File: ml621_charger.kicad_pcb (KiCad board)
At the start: 2 copper layers, 12.2 x 14.5 mm, 9 parts, among them J1 Conn_01x05

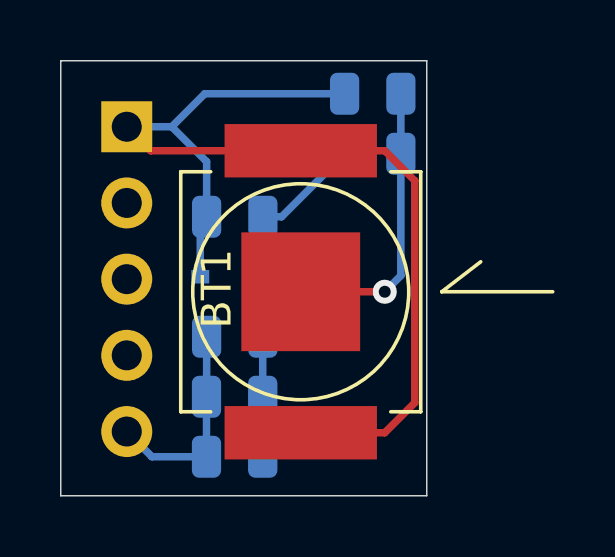
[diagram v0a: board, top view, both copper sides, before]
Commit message: Add schottkey diode to ensure reverse protection
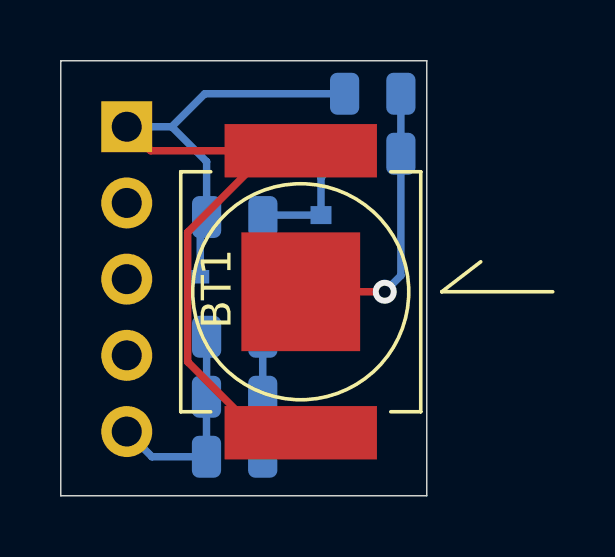
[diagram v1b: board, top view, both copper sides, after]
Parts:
- added D2: 500mV, Diode_SMD:D_SOD-523, B.Cu at (130.2, 93.3)
- R4: value 200R -> 100R
- R5: value 470R -> 330R
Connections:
- D1 pad 1: Net-(C1-Pad1) -> Net-(D1-Pad1)
- R1 pad 1: Net-(C1-Pad1) -> Net-(D1-Pad1)
- R2 pad 1: Net-(C1-Pad1) -> Net-(D1-Pad1)
- R3 pad 1: Net-(C1-Pad1) -> Net-(D1-Pad1)
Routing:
- net Net-(D1-Pad1): track 0.00 -> 8.20 mm
- net Net-(C1-Pad1): track 11.6 -> 4.35 mm
- net /GND: track 35.2 -> 33.4 mm

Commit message: Fix battery holder polarity
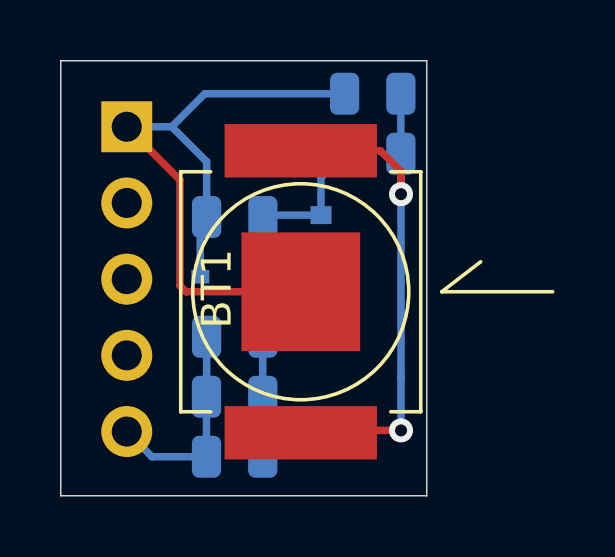
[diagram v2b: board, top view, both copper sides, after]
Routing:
- net Net-(BT1-Pad1): track 9.62 -> 21.4 mm, vias 1 -> 2
- net /GND: track 33.4 -> 23.4 mm
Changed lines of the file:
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@@
     (thickness 1.6)
     (drawings 4)
-    (tracks 36)
+    (tracks 42)
     (zones 0)
     (modules 10)
@@
     (add_net "Net-(J1-Pad4)")
   )
+  (module Battery:BatteryHolder_Keystone_2998_621_6.8x2.2mm (layer F.Cu)
+    (at 129.5 95.2 270)
+    (fp_text reference BT1 (at -0.1 2.8 90) (layer F.SilkS)
+      (effects (font (size 1 1) (thickness 0.15)))
+    )
+    (fp_text value ML621 (at 0.1 6.4 90) (layer F.Fab)
+      (effects (font (size 1 1) (thickness 0.15)))
+    )
+    (fp_line (start 4 4) (end 4 3) (layer F.SilkS) (width 0.12))
+    (fp_line (start -4 4) (end -4 3) (layer F.SilkS) (width 0.12))
+    (fp_line (start 4 -4) (end 4 -3) (layer F.SilkS) (width 0.12))
+    (fp_line (start -4 -4) (end -4 -3) (layer F.SilkS) (width 0.12))
+    (fp_line (start 0 -4.7) (end -1 -6) (layer F.SilkS) (width 0.12))
+    (fp_line (start 0 -8.4) (end 0 -4.7) (layer F.SilkS) (width 0.12))
+    (fp_line (start 4 4) (end -4 4) (layer F.SilkS) (width 0.12))
+    (fp_line (start -4 -4) (end 4 -4) (layer F.SilkS) (width 0.12))
+    (fp_circle (center 0 0) (end 3.6 0) (layer F.SilkS) (width 0.12))
+    (pad 1 smd rect (at 4.7 0 270) (size 1.78 5.08) (layers F.Cu F.Paste F.Mask)
+      (net 2 "Net-(BT1-Pad1)"))
+    (pad 1 smd rect (at -4.7 0 270) (size 1.78 5.08) (layers F.Cu F.Paste F.Mask)
+      (net 2 "Net-(BT1-Pad1)"))
+    (pad 2 smd rect (at 0 0 270) (size 3.96 3.96) (layers F.Cu F.Paste F.Mask)
+      (net 1 /GND))
+  )
   (module Diode_SMD:D_SOD-523 (layer B.Cu)
     (at 130.175 93.345 270)
@@
     )
   )
-  (module Battery:BatteryHolder_Keystone_2998_621_6.8x2.2mm (layer F.Cu)
-    (at 129.5 95.2 270)
-    (fp_text reference BT1 (at -0.1 2.8 90) (layer F.SilkS)
-      (effects (font (size 1 1) (thickness 0.15)))
-    )
-    (fp_text value ML621 (at 0.1 6.4 90) (layer F.Fab)
-      (effects (font (size 1 1) (thickness 0.15)))
-    )
-    (fp_line (start 4 4) (end 4 3) (layer F.SilkS) (width 0.12))
-    (fp_line (start -4 4) (end -4 3) (layer F.SilkS) (width 0.12))
-    (fp_line (start 4 -4) (end 4 -3) (layer F.SilkS) (width 0.12))
-    (fp_line (start -4 -4) (end -4 -3) (layer F.SilkS) (width 0.12))
-    (fp_line (start 0 -4.7) (end -1 -6) (layer F.SilkS) (width 0.12))
-    (fp_line (start 0 -8.4) (end 0 -4.7) (layer F.SilkS) (width 0.12))
-    (fp_line (start 4 4) (end -4 4) (layer F.SilkS) (width 0.12))
-    (fp_line (start -4 -4) (end 4 -4) (layer F.SilkS) (width 0.12))
-    (fp_circle (center 0 0) (end 3.6 0) (layer F.SilkS) (width 0.12))
-    (pad 2 smd rect (at 4.7 0 270) (size 1.78 5.08) (layers F.Cu F.Paste F.Mask)
-      (net 1 /GND))
-    (pad 2 smd rect (at -4.7 0 270) (size 1.78 5.08) (layers F.Cu F.Paste F.Mask)
-      (net 1 /GND))
-    (pad 1 smd rect (at 0 0 270) (size 3.96 3.96) (layers F.Cu F.Paste F.Mask)
-      (net 2 "Net-(BT1-Pad1)"))
-  )
   (module Resistor_SMD:R_0805_2012Metric (layer B.Cu)
     (at 131.9 88.6 180)
@@
   (gr_line (start 121.5 102) (end 133.7 102) (layer Edge.Cuts) (width 0.05))
   (gr_line (start 121.5 87.5) (end 121.5 102) (layer Edge.Cuts) (width 0.05))
-  (segment (start 124.5 90.5) (end 123.7 89.7) (width 0.25) (layer F.Cu) (net 1))
-  (segment (start 129.5 90.5) (end 124.5 90.5) (width 0.25) (layer F.Cu) (net 1))
   (segment (start 125.2 89.7) (end 123.7 89.7) (width 0.25) (layer B.Cu) (net 1))
   (segment (start 126.3 88.6) (end 125.2 89.7) (width 0.25) (layer B.Cu) (net 1))
@@
   (segment (start 126.3625 90.8625) (end 125.2 89.7) (width 0.25) (layer B.Cu) (net 1))
   (segment (start 126.3625 92.71) (end 126.3625 90.8625) (width 0.25) (layer B.Cu) (net 1))
-  (segment (start 129.5 99.9) (end 128.094 99.9) (width 0.25) (layer F.Cu) (net 1))
-  (segment (start 128.094 99.9) (end 125.73 97.536) (width 0.25) (layer F.Cu) (net 1))
-  (segment (start 129.5 90.5) (end 128.448 90.5) (width 0.25) (layer F.Cu) (net 1))
-  (segment (start 125.73 93.218) (end 125.73 97.536) (width 0.25) (layer F.Cu) (net 1))
-  (segment (start 128.448 90.5) (end 125.73 93.218) (width 0.25) (layer F.Cu) (net 1))
-  (via (at 132.3 95.2) (size 0.8) (drill 0.4) (layers F.Cu B.Cu) (net 2))
-  (segment (start 129.5 95.2) (end 132.3 95.2) (width 0.25) (layer F.Cu) (net 2))
-  (segment (start 132.8375 94.6625) (end 132.3 95.2) (width 0.25) (layer B.Cu) (net 2))
-  (segment (start 132.8375 90.6) (end 132.8375 94.6625) (width 0.25) (layer B.Cu) (net 2))
+  (segment (start 129.5 95.2) (end 125.68 95.2) (width 0.25) (layer F.Cu) (net 1))
+  (segment (start 125.68 95.2) (end 125.476 94.996) (width 0.25) (layer F.Cu) (net 1))
+  (segment (start 125.476 91.476) (end 123.7 89.7) (width 0.25) (layer F.Cu) (net 1))
+  (segment (start 125.476 94.996) (end 125.476 91.476) (width 0.25) (layer F.Cu) (net 1))
+  (segment (start 129.5 99.9) (end 128.094 99.9) (width 0.25) (layer F.Cu) (net 2))
+  (segment (start 129.5 90.5) (end 128.448 90.5) (width 0.25) (layer F.Cu) (net 2))
   (segment (start 132.8375 90.6) (end 132.8375 88.6) (width 0.25) (layer B.Cu) (net 2))
+  (segment (start 129.5 90.5) (end 132.156 90.5) (width 0.25) (layer F.Cu) (net 2))
+  (via (at 132.842 91.948) (size 0.8) (drill 0.4) (layers F.Cu B.Cu) (net 2))
+  (segment (start 132.156 90.5) (end 132.842 91.186) (width 0.25) (layer F.Cu) (net 2))
+  (segment (start 132.842 91.186) (end 132.842 91.948) (width 0.25) (layer F.Cu) (net 2))
+  (segment (start 132.842 90.6045) (end 132.8375 90.6) (width 0.25) (layer B.Cu) (net 2))
+  (segment (start 132.842 91.948) (end 132.842 90.6045) (width 0.25) (layer B.Cu) (net 2))
+  (segment (start 132.842 91.948) (end 132.842 98.044) (width 0.25) (layer B.Cu) (net 2))
+  (via (at 132.842 99.822) (size 0.8) (drill 0.4) (layers F.Cu B.Cu) (net 2))
+  (segment (start 132.842 98.044) (end 132.842 99.822) (width 0.25) (layer B.Cu) (net 2))
+  (segment (start 129.578 99.822) (end 129.5 99.9) (width 0.25) (layer F.Cu) (net 2))
+  (segment (start 132.842 99.822) (end 129.578 99.822) (width 0.25) (layer F.Cu) (net 2))
   (segment (start 128.25 92.7125) (end 128.2375 92.7) (width 0.25) (layer B.Cu) (net 3))
   (segment (start 128.3025 92.645) (end 128.2375 92.71) (width 0.25) (layer B.Cu) (net 3))
@@
   (segment (start 130.175 91.3875) (end 130.9625 90.6) (width 0.25) (layer B.Cu) (net 3))
   (segment (start 130.175 92.645) (end 130.175 91.3875) (width 0.25) (layer B.Cu) (net 3))
+  (segment (start 124.54 100.7) (end 123.7 99.86) (width 0.25) (layer B.Cu) (net 4))
+  (segment (start 126.357499 100.7) (end 124.54 100.7) (width 0.25) (layer B.Cu) (net 4))
+  (segment (start 126.357499 98.7) (end 126.357499 100.7) (width 0.25) (layer B.Cu) (net 4))
+  (segment (start 126.3625 98.694999) (end 126.357499 98.7) (width 0.25) (layer B.Cu) (net 4))
+  (segment (start 126.3625 96.7) (end 126.3625 98.694999) (width 0.25) (layer B.Cu) (net 4))
   (segment (start 128.2375 94.7125) (end 128.25 94.7) (width 0.25) (layer B.Cu) (net 8))
   (segment (start 128.2375 96.7) (end 128.2375 94.7125) (width 0.25) (layer B.Cu) (net 8))
@@
   (segment (start 128.232499 96.705001) (end 128.2375 96.7) (width 0.25) (layer B.Cu) (net 8))
   (segment (start 128.232499 98.7) (end 128.232499 96.705001) (width 0.25) (layer B.Cu) (net 8))
-  (segment (start 124.54 100.7) (end 123.7 99.86) (width 0.25) (layer B.Cu) (net 4))
-  (segment (start 126.357499 100.7) (end 124.54 100.7) (width 0.25) (layer B.Cu) (net 4))
-  (segment (start 126.357499 98.7) (end 126.357499 100.7) (width 0.25) (layer B.Cu) (net 4))
-  (segment (start 126.3625 98.694999) (end 126.357499 98.7) (width 0.25) (layer B.Cu) (net 4))
-  (segment (start 126.3625 96.7) (end 126.3625 98.694999) (width 0.25) (layer B.Cu) (net 4))
   (segment (start 129.52 94.7) (end 130.175 94.045) (width 0.25) (layer B.Cu) (net 8))
   (segment (start 128.25 94.7) (end 129.52 94.7) (width 0.25) (layer B.Cu) (net 8))

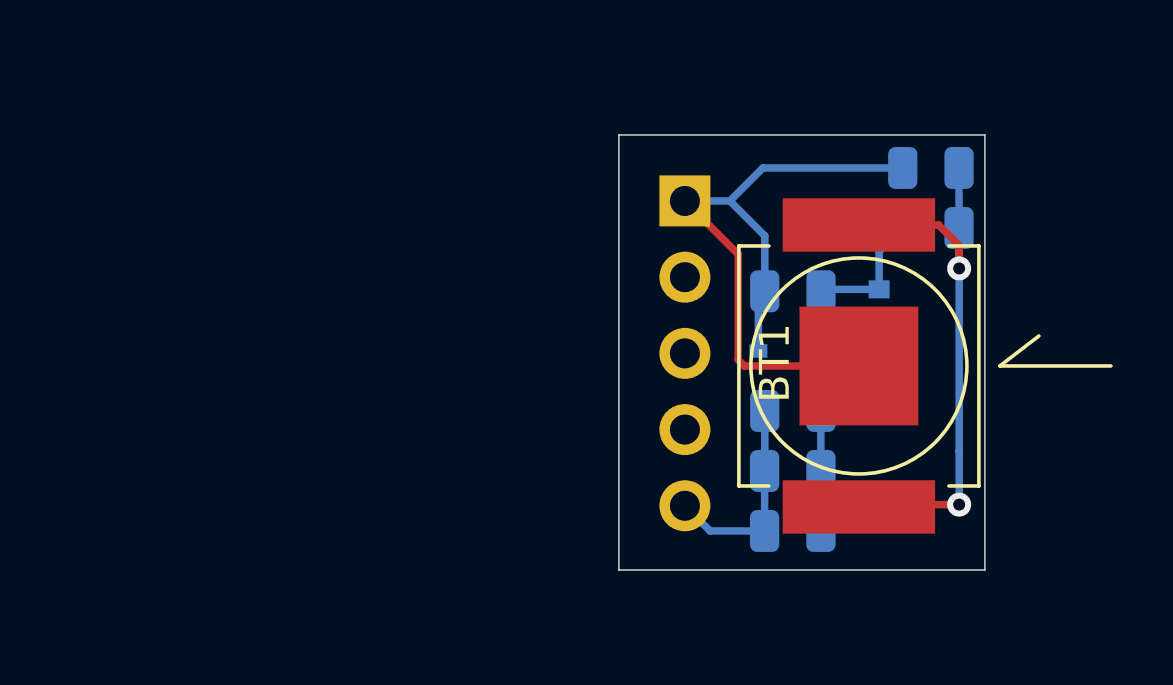
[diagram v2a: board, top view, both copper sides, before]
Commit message: Put USB connector directly on; add indicator LEDs
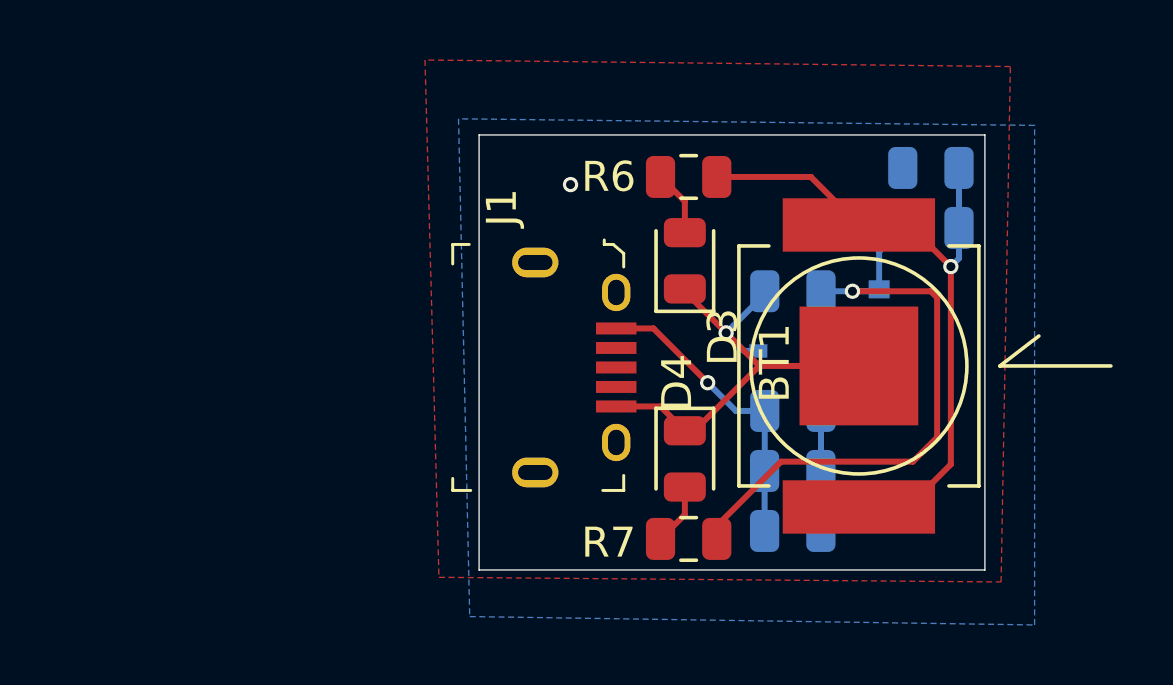
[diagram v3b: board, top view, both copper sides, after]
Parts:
- added D3: LED_3v_GRN, LED_SMD:LED_0805_2012Metric, F.Cu at (123.7, 91.7)
- added D4: LED_2v_RED, LED_SMD:LED_0805_2012Metric, F.Cu at (123.7, 98.3)
- added R6: 100R, Resistor_SMD:R_0805_2012Metric, F.Cu at (123.8, 88.9)
- added R7: 100R, Resistor_SMD:R_0805_2012Metric, F.Cu at (123.8, 101.0)
- D2: value 500mV -> 200mV
- J1: value Conn_01x05 -> USB_B_Micro; footprint Connector_PinHeader_2.54mm:PinHeader_1x05_P2.54mm_Vertical -> digikey-footprints:USB_Micro_B_Female_10118194-0001LF; moved to F.Cu
- moved J1 6.00 mm to (121.4, 95.2), turned to 270 degrees
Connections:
- J1 pad 1: /GND -> /+4.9-5.4V
- J1 pad 5: /+4.9-5.4V -> /GND
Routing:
- net Net-(C1-Pad1): track 4.35 -> 20.9 mm, vias 0 -> 1
- net /GND: track 23.4 -> 18.1 mm, vias 0 -> 2
- net /+4.9-5.4V: track 7.01 -> 10.1 mm, vias 0 -> 1
- net Net-(D3-Pad2): track 0.00 -> 2.19 mm
- net Net-(D4-Pad2): track 0.00 -> 2.07 mm
- net Net-(BT1-Pad1): track 21.4 -> 22.7 mm, vias 2 -> 1
- added copper zone on B.Cu, net /GND
- added copper zone on F.Cu, net /GND
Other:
- board size 12.2 x 14.5 mm -> 16.9 x 14.5 mm
- board text added: "WM v1.1.0 12/15/19"

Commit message: Change around some values
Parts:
- R1, R2: value 62R -> 10R
- R7: value 100R -> 330R
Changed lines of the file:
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@@
   )
   (setup
-    (last_trace_width 0.2)
+    (last_trace_width 0.25)
     (user_trace_width 0.2)
     (trace_clearance 0.2)
@@
       (effects (font (size 1 1) (thickness 0.15)))
     )
-    (fp_text value 100R (at 0 1.65) (layer F.Fab)
+    (fp_text value 330R (at 0 1.65) (layer F.Fab)
       (effects (font (size 1 1) (thickness 0.15)))
     )
@@
       (effects (font (size 1 1) (thickness 0.15)) (justify mirror))
     )
-    (fp_text value 62R (at -2.499001 -0.106) (layer B.Fab)
+    (fp_text value 10R (at -2.499001 -0.106) (layer B.Fab)
       (effects (font (size 1 1) (thickness 0.15)) (justify mirror))
     )
@@
       (effects (font (size 1 1) (thickness 0.15)) (justify mirror))
     )
-    (fp_text value 62R (at -2.494 -0.074) (layer B.Fab)
-      (effects (font (size 1 1) (thickness 0.15)) (justify mirror))
-    )
+    (fp_text value 10R (at -2.494 -0.074) (layer B.Fab)
+      (effects (font (size 1 1) (thickness 0.15)) (justify mirror))
+    )

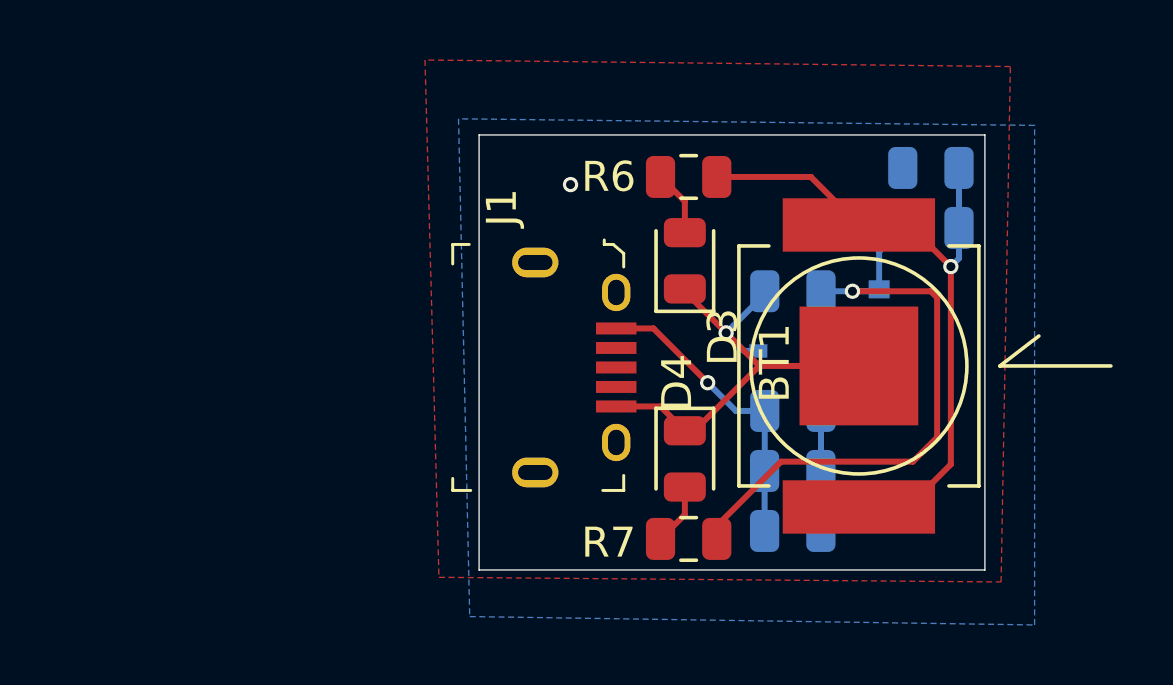
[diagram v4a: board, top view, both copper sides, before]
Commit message: V3 with a microcontroller
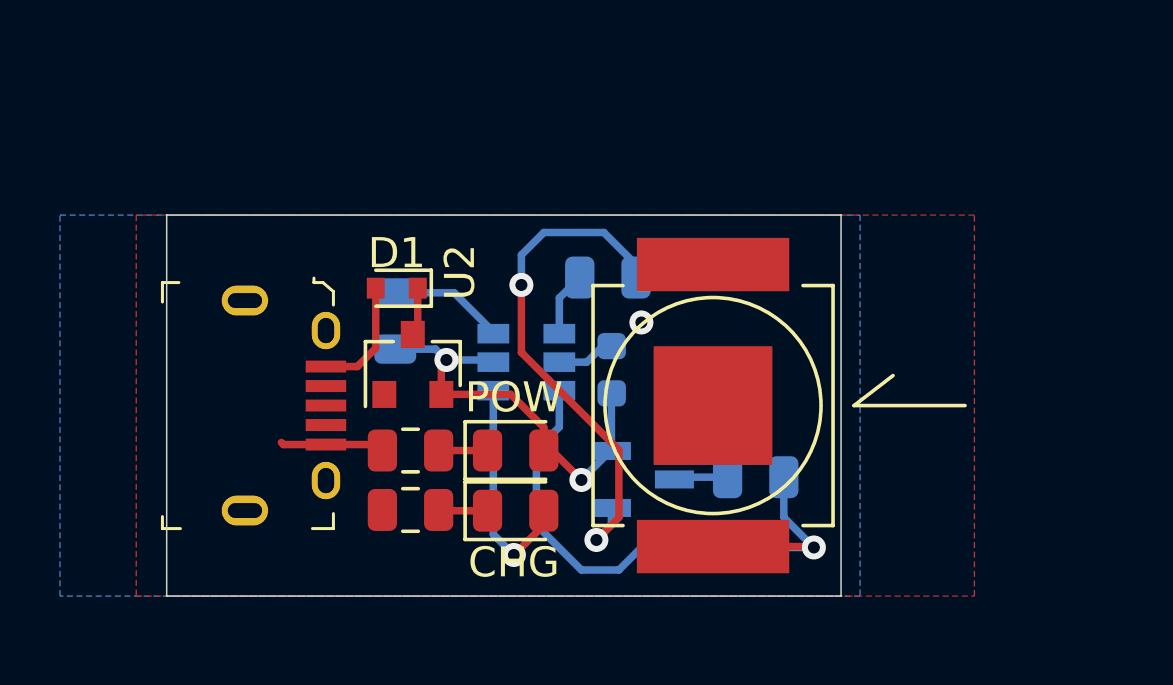
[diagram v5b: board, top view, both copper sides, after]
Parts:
- removed D4: LED_2v_RED, LED_SMD:LED_0805_2012Metric
- removed R6: 100R, Resistor_SMD:R_0805_2012Metric
- removed R7: 330R, Resistor_SMD:R_0805_2012Metric
- added Q1: BSS138, digikey-footprints:SOT-23-3, B.Cu at (122.3, 99.0)
- added REF**: Logo_WM, Symbol:Logo_WM, B.Cu at (109.0, 96.5)
- added U1: ATtiny10-TS, Package_TO_SOT_SMD:SOT-23-6, B.Cu at (118.4, 95.1)
- added U2: AMS1117-3.3, Package_TO_SOT_SMD:SOT-23, F.Cu at (114.6, 95.1)
- C1: value 4.7uF -> 0.1uF; footprint Capacitor_SMD:C_0805_2012Metric -> Capacitor_SMD:C_0603_1608Metric
- D1: value 4.7VRZ -> 500mV; footprint Diode_SMD:D_SOD-323 -> Diode_SMD:D_SOD-523; moved to F.Cu
- D2: value 200mV -> LED; footprint Diode_SMD:D_SOD-523 -> LED_SMD:LED_0805_2012Metric; moved to F.Cu
- D3: value LED_3v_GRN -> LED
- R1: value 10R -> 20R; moved to F.Cu
- R2: value 10R -> 10kR
- R3: value 62R -> 20R; moved to F.Cu
- R4: value 100R -> 20R
- R5: value 330R -> 1kR
- moved R2 14.2 mm to (114.0, 93.7), turned to 270 degrees
- moved D1 13.3 mm to (114.1, 92.6)
- moved D2 13.0 mm to (118.1, 98.0), turned to 0 degrees
- moved R1 12.8 mm to (114.6, 98.0)
- moved R3 12.8 mm to (114.6, 100.0), turned to 0 degrees
- moved R5 11.8 mm to (126.1, 98.9), turned to 0 degrees
- moved R4 10.9 mm to (121.1, 92.3)
- moved D3 10.1 mm to (118.1, 100.0), turned to 0 degrees
- moved J1 9.76 mm to (111.7, 96.5)
- moved C1 6.58 mm to (121.3, 95.3), turned to 90 degrees
- moved BT1 5.04 mm to (124.6, 96.5)
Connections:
- BT1 pad 1: Net-(BT1-Pad1) -> VBAT
- BT1 pad 2: /GND -> GND
- C1 pad 1: Net-(C1-Pad1) -> V_REG
- C1 pad 2: /GND -> GND
- D1 pad 2: /GND -> VSUPPLY
- D2 pad 1: Net-(C1-Pad1) -> Net-(D2-Pad1)
- D2 pad 2: Net-(D1-Pad1) -> V_REG
- D3 pad 1: /GND -> Net-(D3-Pad1)
- J1 pad 1: /+4.9-5.4V -> VSUPPLY
- J1 pad 2: Net-(J1-Pad2) -> (no net)
- J1 pad 3: Net-(J1-Pad3) -> (no net)
- J1 pad 4: Net-(J1-Pad4) -> (no net)
- J1 pad 5: /GND -> GND
- R1 pad 1: Net-(D1-Pad1) -> Net-(D2-Pad1)
- R1 pad 2: /+4.9-5.4V -> GND
- R2 pad 1: Net-(D1-Pad1) -> Net-(R2-Pad1)
- R2 pad 2: /+4.9-5.4V -> V_REG
- R3 pad 1: Net-(D1-Pad1) -> GND
- R3 pad 2: /+4.9-5.4V -> Net-(D3-Pad1)
- R4 pad 1: Net-(C1-Pad1) -> BGATE
- R4 pad 2: Net-(BT1-Pad1) -> Net-(Q1-Pad1)
- R5 pad 1: Net-(BT1-Pad1) -> Net-(Q1-Pad3)
- R5 pad 2: /GND -> VBAT
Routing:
- net Net-(BT1-Pad1): track 22.7 -> 0.00 mm, vias 1 -> 0
- net VBAT: track 0.00 -> 21.1 mm, vias 0 -> 1
- net Net-(C1-Pad1): track 20.9 -> 0.00 mm, vias 1 -> 0
- net /GND: track 18.1 -> 0.00 mm, vias 2 -> 0
- net Net-(Q1-Pad1): track 0.00 -> 17.4 mm, vias 0 -> 2
- net V_REG: track 0.00 -> 14.3 mm, vias 0 -> 2
- net /+4.9-5.4V: track 10.1 -> 0.00 mm, vias 1 -> 0
- net Net-(D1-Pad1): track 8.20 -> 1.61 mm
- net Net-(D3-Pad2): track 2.19 -> 7.65 mm, vias 0 -> 1
- net GND: track 0.00 -> 5.44 mm, vias 0 -> 1
- net VSUPPLY: track 0.00 -> 3.91 mm
- net Net-(R2-Pad1): track 0.00 -> 3.87 mm
- net BGATE: track 0.00 -> 2.15 mm
- net Net-(D4-Pad2): track 2.07 -> 0.00 mm
- net Net-(Q1-Pad3): track 0.00 -> 1.80 mm
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- added copper zone on B.Cu, net GND
- added copper zone on F.Cu, net GND
- removed copper zone on B.Cu, net /GND
- removed copper zone on F.Cu, net /GND
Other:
- board size 16.9 x 14.5 mm -> 22.5 x 12.7 mm
- board text added: "CHG"
- board text added: "POW"
- board text added: "v3.0.0 05/24/20"
- board text removed: "WM v1.1.0 12/15/19"
